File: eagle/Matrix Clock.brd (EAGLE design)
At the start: 153 x 38 mm, 48 parts, among them IC1 MEGA32-A, IC2 LM1117IMPX-3.3, IC3 DS1307Z, IC4 MAX7219CWG, IC5 MAX7219CWG, IC6 MAX7219CWG, IC7 MAX7219CWG, Q1 32768, Q2 16MHz, X1 MINI-USB-SCHIELD-32005-301

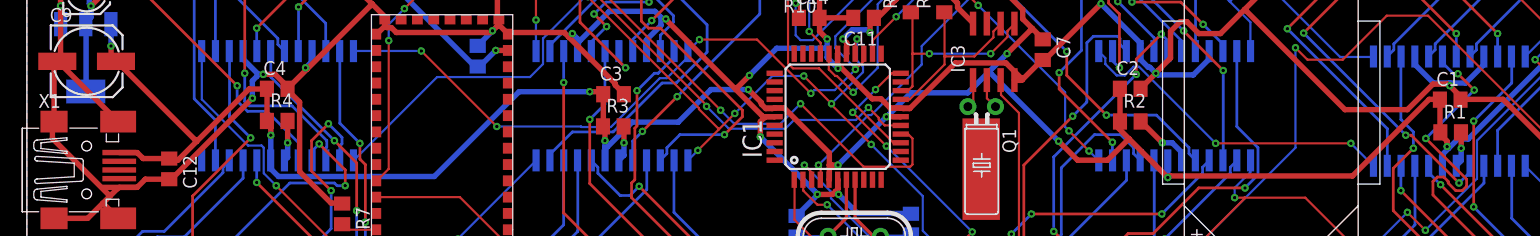
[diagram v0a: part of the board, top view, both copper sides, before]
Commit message: Started clock firmware
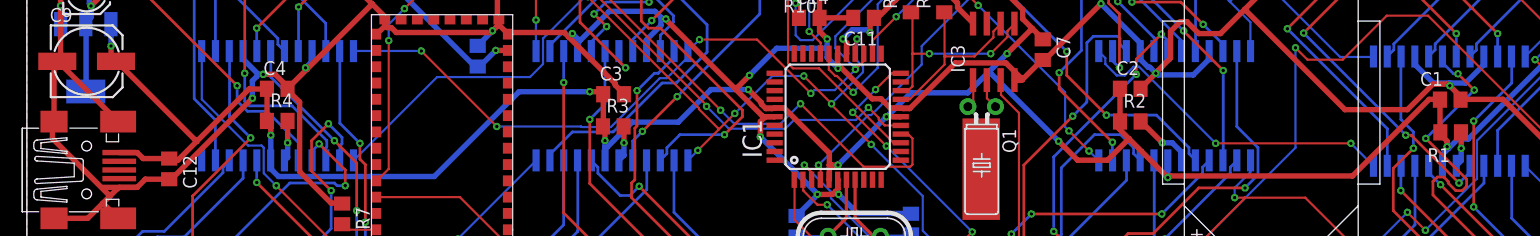
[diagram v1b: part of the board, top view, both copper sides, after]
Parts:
- renumbered U$12 to PR1, U$5 to BAT1
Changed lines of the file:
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@@
 <element name="LED1" library="LED" package="CPD15088" value="CPD-15088YGD2/A" x="152.8" y="38.1" locked="yes" rot="MR0"/>
 <element name="IC4" library="max7219" package="SO24L" value="MAX7219CWG" x="130.91" y="18.41" rot="MR180"/>
-<element name="R1" library="rcl" package="R0805" value="10k" x="131.03" y="16.46"/>
-<element name="C1" library="rcl" package="C0805" value="0.1mf" x="130.99" y="19.47"/>
+<element name="R1" library="rcl" package="R0805" value="10k" x="131.03" y="16.46" smashed="yes">
+<attribute name="NAME" x="128.895" y="13.73" size="1.27" layer="25"/>
+<attribute name="VALUE" x="131.645" y="13.92" size="1.27" layer="27"/>
+</element>
+<element name="C1" library="rcl" package="C0805" value="0.1mf" x="130.99" y="19.47" smashed="yes">
+<attribute name="NAME" x="128.22" y="20.74" size="1.27" layer="25"/>
+<attribute name="VALUE" x="130.72" y="20.93" size="1.27" layer="27"/>
+</element>
 <element name="LED2" library="LED" package="CPD15088" value="CPD-15088YGD2/A" x="114.53" y="38.1" locked="yes" rot="MR0"/>
 <element name="IC5" library="max7219" package="SO24L" value="MAX7219CWG" x="105.63" y="18.91" rot="MR180"/>
@@
 <element name="IC2" library="lm1117" package="SOT223" value="LM1117IMPX-3.3" x="5.42" y="23.32" rot="MR180"/>
 <element name="U$1" library="bc417" package="BTM400_6B" value="" x="38.21" y="13.84" rot="R180"/>
-<element name="U$5" library="misc" package="CR2032-SMD" value="CR2032" x="114.52" y="18.4" rot="R90"/>
+<element name="BAT1" library="misc" package="CR2032-SMD" value="CR2032" x="114.52" y="18.4" rot="R90"/>
 <element name="U$7" library="misc" package="HC0905" value="HC0905" x="147.82" y="9.64" rot="R270"/>
 <element name="U$9" library="misc" package="IT1188E" value="IT1188E" x="22.37" y="36.39" rot="R180"/>
@@
 <element name="C7" library="rcl" package="C0805" value="0.1mf" x="93.49" y="24.07" rot="R270"/>
 <element name="C8" library="rcl" package="C0805" value="0.1mf" x="41.49" y="23.47" rot="MR90"/>
-<element name="U$12" library="misc" package="GL55" value="GL5537" x="72.27" y="34.96" rot="R180"/>
+<element name="PR1" library="misc" package="GL55" value="GL5537" x="72.27" y="34.96" rot="R180"/>
 <element name="R10" library="rcl" package="R0805" value="1M" x="72.04" y="30.02" rot="R180"/>
 <element name="C11" library="rcl" package="C0805" value="0.1mf" x="77" y="27" rot="R180"/>
 <element name="C12" library="rcl" package="C0805" value="0.1mf" x="13.1" y="13.1" rot="R270"/>
-<element name="X1" library="con-cypressindustries" package="32005-301" value="MINI-USB-SCHIELD-32005-301" x="5.5" y="13" locked="yes">
+<element name="X1" library="con-cypressindustries" package="32005-301" value="MINI-USB-SCHIELD-32005-301" x="5.5" y="13" locked="yes" smashed="yes">
 <attribute name="OC_NEWARK" value="unknown" x="5.5" y="13" size="1.778" layer="27" display="off"/>
 <attribute name="MPN" value="" x="5.5" y="13" size="1.778" layer="27" display="off"/>
@@
 <contactref element="U$3" pad="6"/>
 <contactref element="U$7" pad="P$1"/>
-<contactref element="U$5" pad="-"/>
+<contactref element="BAT1" pad="-"/>
 <contactref element="IC2" pad="1"/>
 <contactref element="LED5" pad="C"/>
@@
 <contactref element="R8" pad="2"/>
 <contactref element="R9" pad="2"/>
-<contactref element="U$12" pad="P$1"/>
+<contactref element="PR1" pad="P$1"/>
 <contactref element="C11" pad="1"/>
 <contactref element="C12" pad="1"/>
@@
 <signal name="N$3">
 <contactref element="IC3" pad="3"/>
-<contactref element="U$5" pad="+"/>
+<contactref element="BAT1" pad="+"/>
 <wire x1="89.65" y1="19.9" x2="89.65" y2="21.25" width="0.2032" layer="1"/>
 <wire x1="91.3" y1="18.25" x2="89.65" y2="19.9" width="0.2032" layer="1"/>
@@
 </signal>
 <signal name="SENSOR">
-<contactref element="U$12" pad="P$2"/>
+<contactref element="PR1" pad="P$2"/>
 <contactref element="R10" pad="2"/>
 <contactref element="IC1" pad="30"/>

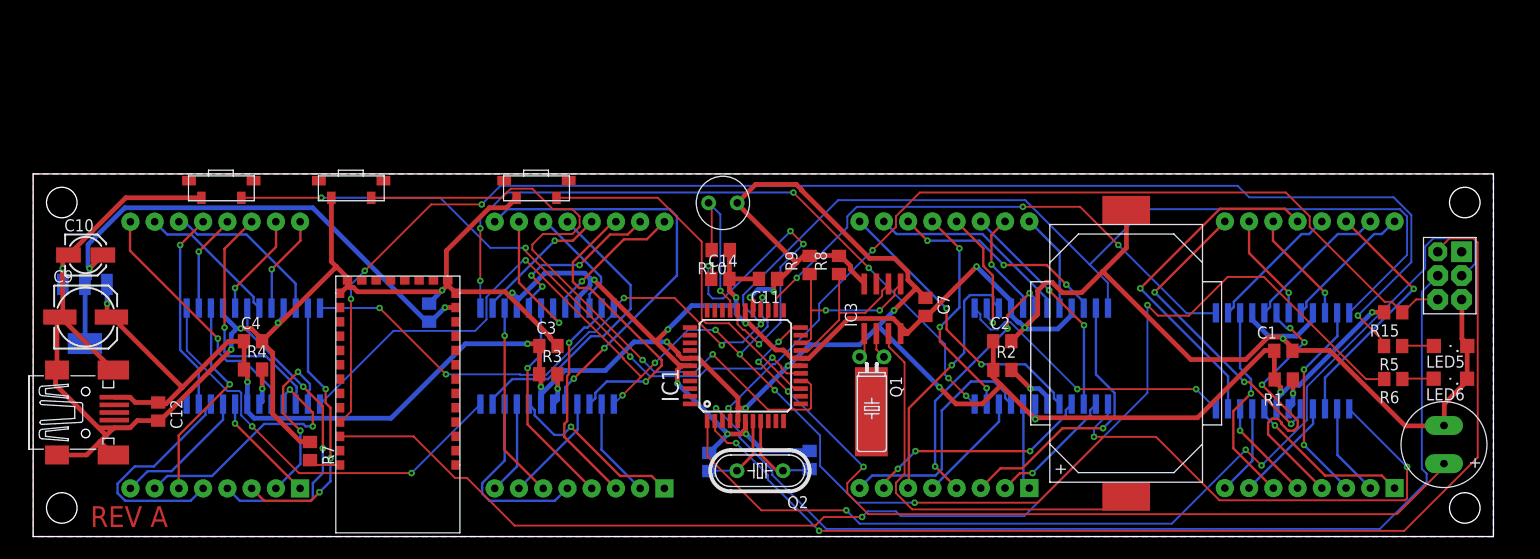
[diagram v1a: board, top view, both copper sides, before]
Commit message: Big update
- Asyncronous USART operations
- Asyncronous ADC
- Updated schematics file and PCB
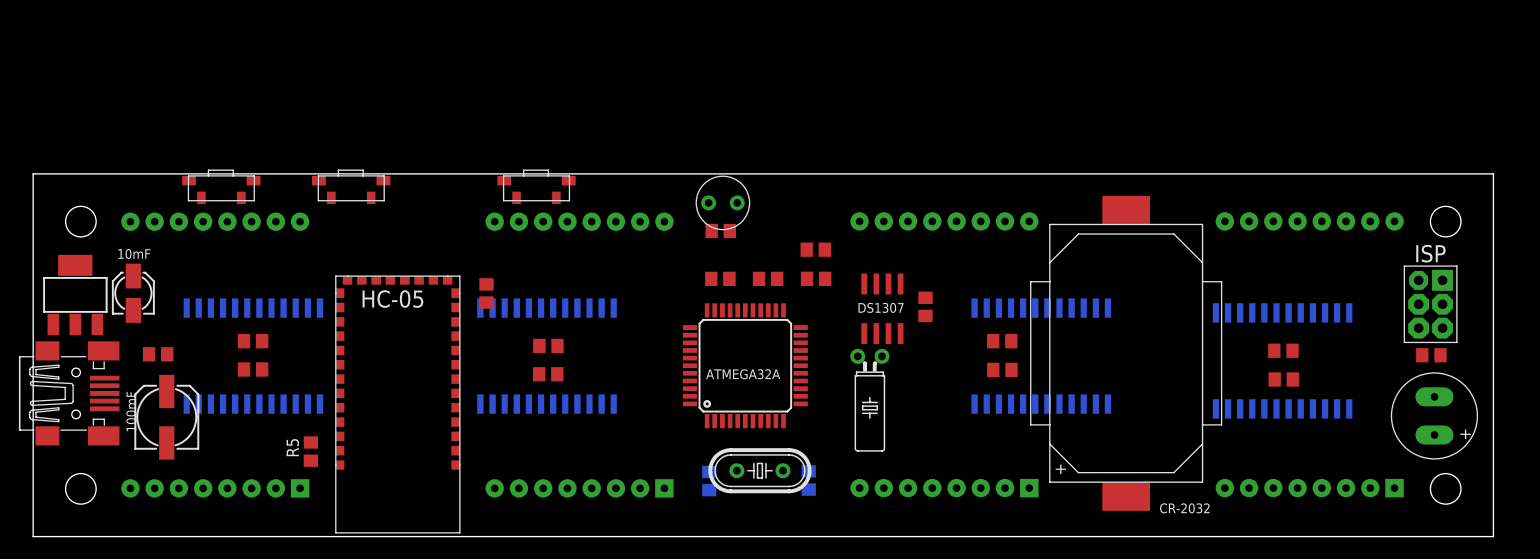
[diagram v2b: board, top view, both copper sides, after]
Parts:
- removed LED5, LED6: (no value), LED:SML1206
- removed R6: 220, rcl:R0805
- removed R7: 10k, rcl:R0805
- R10: value 1M -> 68k
- R5: value 220 -> 4k7
- moved R5 113.9 mm to (29.1, 8.90), turned to 90 degrees
- moved C9 13.5 mm to (14.0, 12.5), turned to 90 degrees
- moved C10 6.40 mm to (10.5, 25.5), turned to 90 degrees
- moved C8 6.32 mm to (47.5, 25.5), flipped to the top
- moved R15 6.02 mm to (146.5, 19.0), turned to 0 degrees
- moved C12 6.00 mm to (13.1, 19.1), turned to 180 degrees
- moved U$3 3.61 mm to (145.2, 24.3)
- moved U$7 3.16 mm to (146.8, 12.6)
- moved R8 2.80 mm to (82.0, 27.0), turned to 180 degrees
- moved IC2 2.24 mm to (4.42, 25.3), flipped to the top, turned to 0 degrees
- moved X1 2.24 mm to (4.50, 15.0)
- moved C6 2.15 mm to (81.3, 5.87), turned to 90 degrees
- moved R10 2.00 mm to (72.0, 32.0)
- moved C5 2.00 mm to (70.8, 5.82), turned to 90 degrees
- moved R9 1.73 mm to (82.0, 30.1), turned to 180 degrees
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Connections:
- removed net RX: U$1.UART-TX
- removed net TX: U$1.UART-RX
- net GND: no longer LED5.C, LED6.C, R7.1
- net N$26: now also IC1.44, U$1.PIO(9); no longer R5.2, U$1.PIO(8)
- net N$27: now also IC1.43, U$1.PIO(8); no longer R6.2, U$1.PIO(9)
- net N$28: now also R5.1; no longer R7.2
- net N$4: now also IC1.10, U$1.UART-RX; no longer LED6.A, R6.1
- net N$5: now also IC1.9, U$1.UART-TX; no longer LED5.A, R5.1
- net VCC: now also R5.2
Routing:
- net GND: track 371.6 -> 0.00 mm, vias 16 -> 0
- net VCC: track 262.0 -> 0.00 mm, vias 14 -> 0
- net DSP-CLK: track 173.5 -> 0.00 mm, vias 10 -> 0
- net DSP-LOAD: track 158.5 -> 0.00 mm, vias 5 -> 0
- net N$26: track 148.7 -> 0.00 mm, vias 4 -> 0
- net N$27: track 135.2 -> 0.00 mm, vias 2 -> 0
- net MISO: track 116.3 -> 0.00 mm, vias 2 -> 0
- net MOSI: track 108.8 -> 0.00 mm, vias 3 -> 0
- net SCK: track 106.6 -> 0.00 mm, vias 1 -> 0
- net RES: track 93.2 -> 0.00 mm, vias 2 -> 0
- net SOUND: track 90.8 -> 0.00 mm, vias 4 -> 0
- net N$14: track 73.4 -> 0.00 mm, vias 6 -> 0
- net BUTTON2: track 72.2 -> 0.00 mm, vias 2 -> 0
- net BUTTON1: track 68.2 -> 0.00 mm, vias 4 -> 0
- net +3V3: track 58.3 -> 0.00 mm, vias 2 -> 0
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- removed copper zone on layer 1, net GND
- removed copper zone on layer 16, net GND
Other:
- board text added: "100mF"
- board text added: "10mF"
- board text added: "ATMEGA32A"
- board text added: "CR-2032"
- board text added: "DS1307"
- board text added: "HC-05"
- board text added: "ISP"
- board text removed: "REV A"

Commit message: Updated schematics and board
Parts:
- removed IC2: LM1117IMPX-3.3, lm1117:SOT223
- added C13: 0.1mf, rcl:C0805
- added R11, R6, R7: 4k7, rcl:R0805
- added U$2: LP2985AIM5-3.3, LP2985:SOT25
- C10: value (none) -> 0.1mf; device rcl:153CLV-0405 -> rcl:C0805
- moved C10 38.3 mm to (48.5, 21.0), turned to 0 degrees
- moved C8 24.8 mm to (72.0, 29.5), turned to 0 degrees
- moved C9 15.0 mm to (5.00, 24.5), turned to 0 degrees
- moved C12 4.27 mm to (11.6, 15.1), turned to 270 degrees
- moved R9 0.50 mm to (82.0, 29.6)
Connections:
- new net BT_ENABLE: IC1.42, U$2.3
- new net BYPASS: C13.1, U$2.4
- net +3V3: now also C10.1, U$2.5; no longer C10.+, C8.1, IC2.2, IC2.TAB
- net BUTTON1: now also IC1.37, R6.1; no longer IC1.16
- net BUTTON2: now also IC1.36, R11.1; no longer IC1.15
- net BUTTON3: now also IC1.35, R7.1
- net GND: now also C10.2, C13.2, U$2.2; no longer C10.-, IC2.1
- net SENSOR: now also C8.1
- net VCC: now also R11.2, R6.2, R7.2, U$2.1; no longer IC2.3
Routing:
- net GND: track 0.00 -> 354.0 mm, vias 0 -> 20
- net VCC: track 0.00 -> 248.6 mm, vias 0 -> 14
- net DSP-LOAD: track 0.00 -> 156.4 mm, vias 0 -> 9
- net DSP-CLK: track 0.00 -> 147.6 mm, vias 0 -> 9
- net RES: track 0.00 -> 106.4 mm
- net SCK: track 0.00 -> 100.3 mm, vias 0 -> 2
- net MOSI: track 0.00 -> 98.2 mm, vias 0 -> 2
- net MISO: track 0.00 -> 96.0 mm, vias 0 -> 3
- net SOUND: track 0.00 -> 90.9 mm, vias 0 -> 2
- net N$14: track 0.00 -> 71.2 mm, vias 0 -> 2
- net BUTTON1: track 0.00 -> 62.1 mm, vias 0 -> 3
- net BT_ENABLE: track 0.00 -> 53.8 mm, vias 0 -> 2
- net BUTTON3: track 0.00 -> 51.3 mm, vias 0 -> 2
- net DSP-DATA: track 0.00 -> 51.2 mm, vias 0 -> 3
- net BUTTON2: track 0.00 -> 49.9 mm, vias 0 -> 2
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- added copper zone on layer 1, net GND
- added copper zone on layer 16, net GND
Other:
- board text added: "REV B"

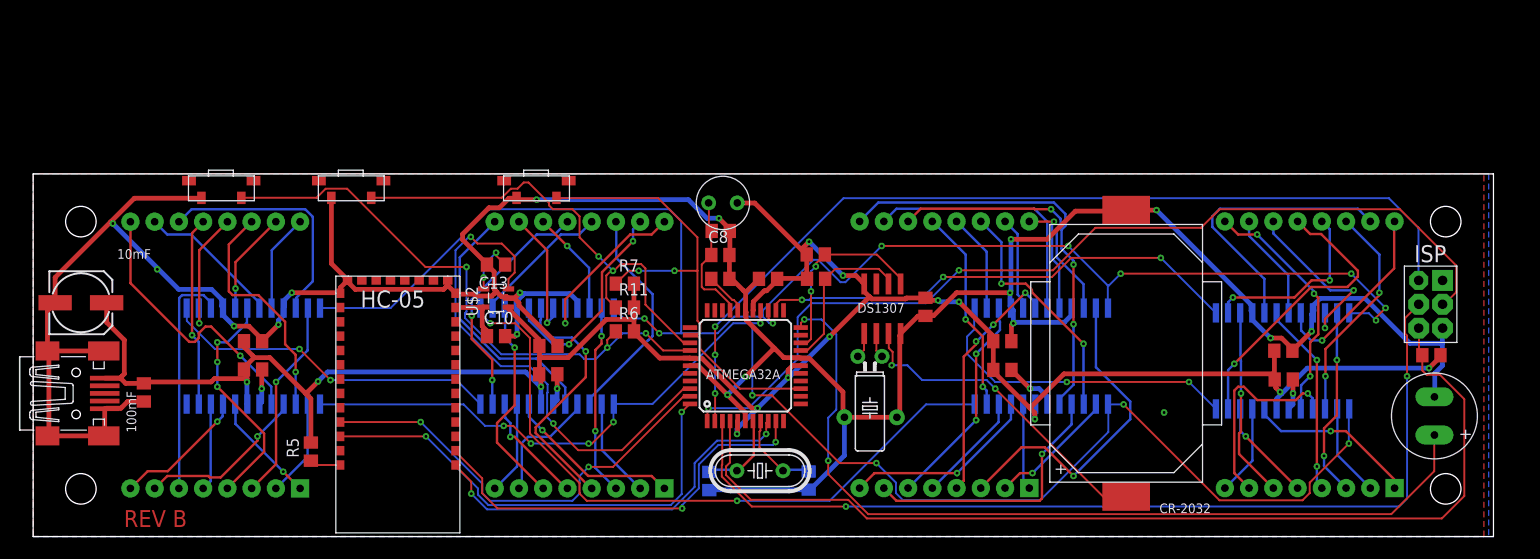
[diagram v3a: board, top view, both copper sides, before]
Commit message: Removed outdated elements
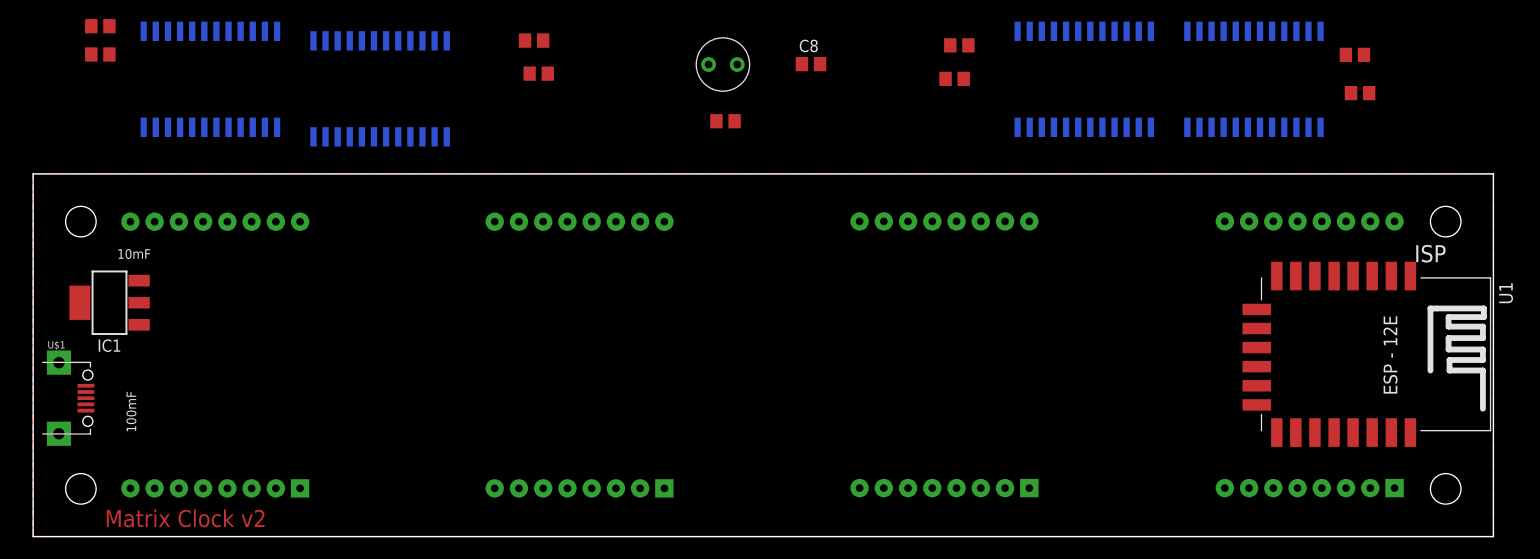
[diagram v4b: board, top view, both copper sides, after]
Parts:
- removed BAT1: CR2032, misc:CR2032-SMD
- removed C10, C11, C12, C13, C14, C7: 0.1mf, rcl:C0805
- removed C5, C6: 22, rcl:C0805
- removed C9: (no value), rcl:153CLV-0605
- removed IC3: DS1307Z, ds1307_pcf8583:SOIC8
- removed Q1: 32768, crystal:TC38H
- removed Q2: 16MHz, crystal:HC49/S
- removed R11, R5, R6, R7, R8, R9: 4k7, rcl:R0805
- removed R15: 1K, rcl:R0805
- removed U$10, U$11, U$9: IT1188E, misc:IT1188E
- removed U$2: LP2985AIM5-3.3, LP2985:SOT25
- removed U$3: AVR-ISP, misc:AVR-ISP
- removed U$7: HC0905, misc:HC0905
- removed X1: MINI-USB-SCHIELD-32005-301, con-cypressindustries:32005-301
- added U1: (no value), esp8266modules:ESP12E-SMD
- IC1: value MEGA32-A -> LM1117MPX-3.3; device avr-7:TQFP44 -> lm1117:SOT223
- U$1: value (none) -> MICRO-USB; device bc417:BTM400_6B -> microusb:MICRO-USB
- moved IC1 66.9 mm to (8.00, 24.5)
- moved U$1 37.2 mm to (1.00, 14.5), turned to 270 degrees
- moved C4 36.7 mm to (7.04, 53.5)
- moved R4 36.7 mm to (7.04, 50.5)
- moved IC6 33.0 mm to (36.4, 46.9)
- moved C3 32.0 mm to (52.5, 52.0)
- moved C1 31.9 mm to (138.5, 50.5)
- moved R3 31.5 mm to (53.0, 48.5)
- moved C2 31.3 mm to (97.0, 51.5)
- moved R1 31.0 mm to (139.0, 46.5)
- moved R2 30.9 mm to (96.5, 48.0)
- moved IC4 29.7 mm to (127.9, 47.9)
- moved IC5 29.3 mm to (110.1, 47.9)
- moved IC7 29.3 mm to (18.6, 47.9)
- moved C8 22.1 mm to (81.5, 49.5)
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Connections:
- removed net BT_ENABLE: IC1.42, U$2.3
- removed net BUTTON1: IC1.37, R6.1, U$9.3
- removed net BUTTON2: IC1.36, R11.1, U$10.3
- removed net BUTTON3: IC1.14, IC1.35, R7.1, U$11.3
- removed net BYPASS: C13.1, U$2.4
- removed net MISO: IC1.2, U$3.1
- removed net MOSI: IC1.1, U$3.4
- removed net N$26: IC1.44, U$1.PIO(9)
- removed net N$27: IC1.43, U$1.PIO(8)
- removed net N$28: R5.1, U$1.PIO(11)
- removed net N$3: BAT1.+, IC3.3
- removed net N$4: IC1.10, U$1.UART-RX
- removed net N$5: IC1.9, U$1.UART-TX
- removed net N$53: IC3.1, Q1.2
- removed net N$54: IC3.2, Q1.1
- removed net N$55: C14.1, IC1.29
- removed net RES: IC1.4, R15.1, U$3.5
- removed net SCK: IC1.3, U$3.3
- removed net SCL: IC1.19, IC3.6, R8.1
- removed net SDA: IC1.20, IC3.5, R9.1
- removed net SOUND: IC1.22, U$7.P$2
- removed net USB-D+: X1.3
- removed net USB-D-: X1.2
- removed net VCC: C1.1, C11.1, C12.1, C2.1, C3.1, C4.1, C7.1, C9.+, IC1.17, IC1.27, IC1.38, IC1.5, IC3.8, IC4.19, IC5.19, IC6.19, IC7.19, PR1.P$1, R1.1, R11.2, R15.2, R2.1, R3.1, R4.1, R5.2, R6.2, R7.2, R8.2, R9.2, U$2.1, X1.1
- removed net XTAL1: C6.2, IC1.8, Q2.1
- removed net XTAL2: C5.2, IC1.7, Q2.2
- new net +5V: C1.1, C2.1, C3.1, C4.1, IC1.3, IC4.19, IC5.19, IC6.19, IC7.19, R1.1, R2.1, R3.1, R4.1, U$1.1
- new net RESET: U1.RESET
- net +3V3: now also IC1.2, IC1.TAB, PR1.P$1, U1.VCC; no longer C10.1, U$1.3.3V, U$2.5
- net DSP-CLK: no longer IC1.26
- net DSP-DATA: no longer IC1.24
- net DSP-LOAD: no longer IC1.25
- net GND: now also IC1.1, U$1.5, U$1.GND1, U$1.GND2, U1.GND; no longer BAT1.-, C10.2, C11.2, C12.2, C13.2, C14.2, C5.1, C6.1, C7.2, C9.-, IC1.18, IC1.28, IC1.39, IC1.6, IC3.4, U$1.GND@1, U$1.GND@2, U$1.GND@3, U$1.GND@4, U$10.4, U$11.4, U$2.2, U$3.6, U$7.P$1, U$9.4, X1.5, X1.M1, X1.M2, X1.M3, X1.M4
- net SENSOR: now also U1.ADC; no longer IC1.30
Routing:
- net GND: track 354.0 -> 0.00 mm, vias 20 -> 0
- net VCC: track 248.6 -> 0.00 mm, vias 14 -> 0
- net DSP-LOAD: track 156.4 -> 0.00 mm, vias 9 -> 0
- net DSP-CLK: track 147.6 -> 0.00 mm, vias 9 -> 0
- net RES: track 106.4 -> 0.00 mm
- net SCK: track 100.3 -> 0.00 mm, vias 2 -> 0
- net MOSI: track 98.2 -> 0.00 mm, vias 2 -> 0
- net MISO: track 96.0 -> 0.00 mm, vias 3 -> 0
- net SOUND: track 90.9 -> 0.00 mm, vias 2 -> 0
- net N$14: track 71.2 -> 0.00 mm, vias 2 -> 0
- net BUTTON1: track 62.1 -> 0.00 mm, vias 3 -> 0
- net BT_ENABLE: track 53.8 -> 0.00 mm, vias 2 -> 0
- net BUTTON3: track 51.3 -> 0.00 mm, vias 2 -> 0
- net DSP-DATA: track 51.2 -> 0.00 mm, vias 3 -> 0
- net BUTTON2: track 49.9 -> 0.00 mm, vias 2 -> 0
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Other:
- board text added: "Matrix Clock v2"
- board text removed: "ATMEGA32A"
- board text removed: "CR-2032"
- board text removed: "DS1307"
- board text removed: "HC-05"
- board text removed: "REV B"
